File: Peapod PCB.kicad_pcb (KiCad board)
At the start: 2 copper layers, 70.9 x 26.9 mm, 20 parts, among them U1 ESP8266

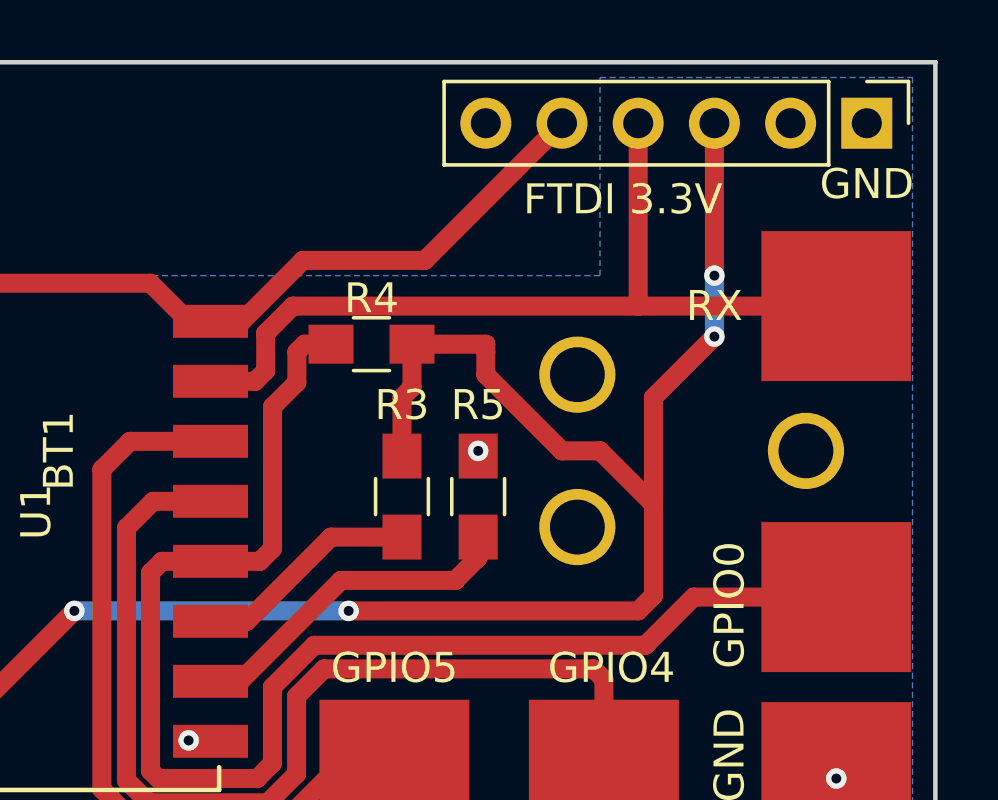
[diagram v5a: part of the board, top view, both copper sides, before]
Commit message: Moved Via
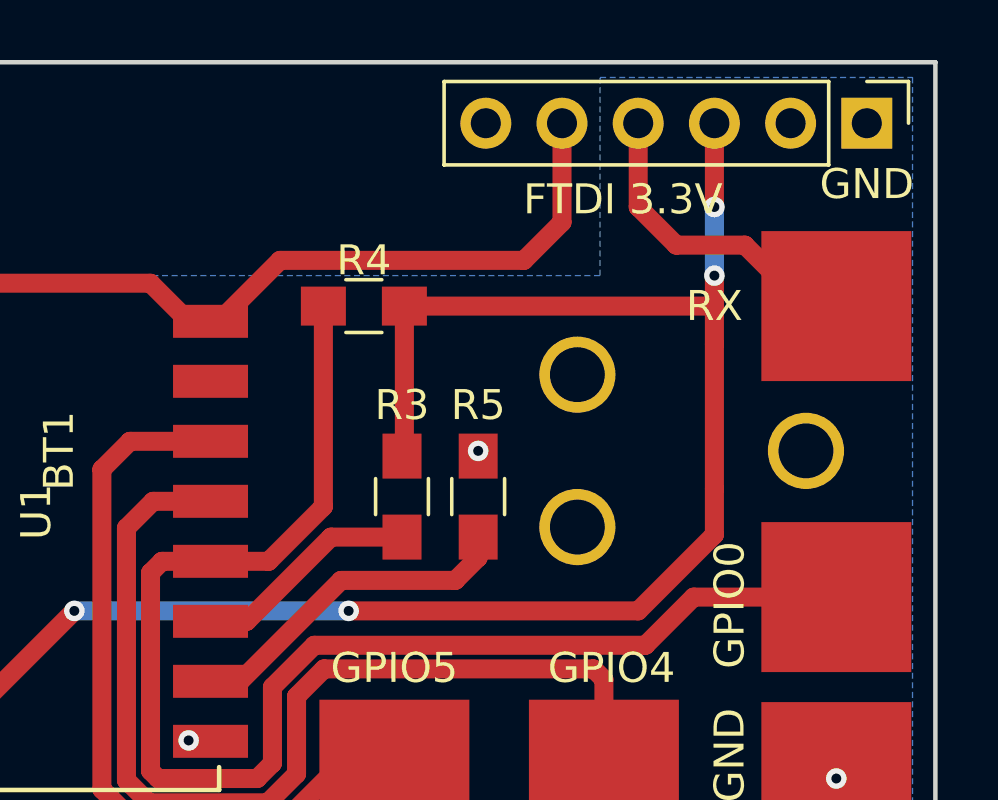
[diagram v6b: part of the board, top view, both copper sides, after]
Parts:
- moved R4 1.30 mm to (204.7, 34.5)
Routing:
- net Net-(J3-Pad4): track 30.7 -> 10.8 mm
- net Net-(J3-Pad5): track 41.9 -> 43.8 mm
- net +3V3: track 140.8 -> 141.7 mm
- net Net-(J7-Pad1): track 46.1 -> 46.9 mm
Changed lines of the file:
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@@
   (general
     (links 42)
-    (no_connects 0)
-    (area 150.970267 23.462266 225.457734 53.415001)
+    (no_connects 1)
+    (area 152.832999 26.340999 223.849001 53.415001)
     (thickness 1.6002)
     (drawings 9)
-    (tracks 157)
+    (tracks 147)
     (zones 0)
     (modules 20)
@@
   )
   (module Resistors_SMD:R_0805_HandSoldering (layer F.Cu)
-    (at 204.978 35.814)
+    (at 204.724 34.544)
     (descr "Resistor SMD 0805, hand soldering")
     (tags "resistor 0805")
@@
     (effects (font (size 6 7) (thickness 0.3)) (justify mirror))
   )
+  (segment (start 206.074 34.544) (end 216.408 34.544) (width 0.635) (layer F.Cu) (net 1) (status 400000))
+  (segment (start 216.408 34.544) (end 216.408 34.798) (width 0.635) (layer F.Cu) (net 1))
+  (segment (start 206.074 34.544) (end 206.074 39.464) (width 0.635) (layer F.Cu) (net 1) (status C00000))
+  (segment (start 206.074 39.464) (end 205.994 39.544) (width 0.635) (layer F.Cu) (net 1) (status C00000))
   (segment (start 184.912 49.052) (end 190.754 49.022) (width 0.635) (layer F.Cu) (net 1))
+  (segment (start 216.408 35.814) (end 216.408 34.798) (width 0.635) (layer F.Cu) (net 1))
+  (segment (start 216.408 40.64) (end 216.408 35.814) (width 0.635) (layer F.Cu) (net 1))
+  (segment (start 216.408 42.164) (end 216.408 40.64) (width 0.635) (layer F.Cu) (net 1))
+  (segment (start 213.868 44.704) (end 216.408 42.164) (width 0.635) (layer F.Cu) (net 1))
+  (segment (start 204.216 44.704) (end 213.868 44.704) (width 0.635) (layer F.Cu) (net 1))
+  (via (at 204.216 44.704) (size 0.6858) (drill 0.3302) (layers F.Cu B.Cu) (net 1))
+  (segment (start 195.072 44.704) (end 204.216 44.704) (width 0.635) (layer B.Cu) (net 1))
+  (via (at 195.072 44.704) (size 0.6858) (drill 0.3302) (layers F.Cu B.Cu) (net 1))
   (segment (start 190.754 49.022) (end 195.072 44.704) (width 0.635) (layer F.Cu) (net 1))
-  (via (at 195.072 44.704) (size 0.6858) (drill 0.3302) (layers F.Cu B.Cu) (net 1))
-  (segment (start 195.072 44.704) (end 204.216 44.704) (width 0.635) (layer B.Cu) (net 1))
-  (via (at 204.216 44.704) (size 0.6858) (drill 0.3302) (layers F.Cu B.Cu) (net 1))
-  (segment (start 204.216 44.704) (end 213.868 44.704) (width 0.635) (layer F.Cu) (net 1))
-  (segment (start 213.868 44.704) (end 214.376 44.196) (width 0.635) (layer F.Cu) (net 1))
-  (segment (start 214.376 44.196) (end 214.376 41.148) (width 0.635) (layer F.Cu) (net 1))
   (segment (start 163.96 41.91) (end 171.958 41.91) (width 0.635) (layer F.Cu) (net 1))
   (segment (start 174.816 39.052) (end 184.912 39.052) (width 0.635) (layer F.Cu) (net 1))
   (segment (start 171.958 41.91) (end 174.816 39.052) (width 0.635) (layer F.Cu) (net 1))
-  (segment (start 214.376 41.148) (end 214.376 37.592) (width 0.635) (layer F.Cu) (net 1))
-  (segment (start 214.376 37.592) (end 216.408 35.56) (width 0.635) (layer F.Cu) (net 1))
-  (via (at 216.408 35.56) (size 0.6858) (drill 0.3302) (layers F.Cu B.Cu) (net 1))
-  (segment (start 216.408 35.56) (end 216.408 33.528) (width 0.635) (layer B.Cu) (net 1))
+  (segment (start 216.408 34.798) (end 216.408 33.528) (width 0.635) (layer F.Cu) (net 1))
+  (segment (start 216.408 31.242) (end 216.408 28.448) (width 0.635) (layer F.Cu) (net 1) (status 800000))
+  (via (at 216.408 31.242) (size 0.6858) (drill 0.3302) (layers F.Cu B.Cu) (net 1))
+  (segment (start 216.408 33.528) (end 216.408 31.242) (width 0.635) (layer B.Cu) (net 1))
   (via (at 216.408 33.528) (size 0.6858) (drill 0.3302) (layers F.Cu B.Cu) (net 1))
-  (segment (start 216.408 33.528) (end 216.408 28.448) (width 0.635) (layer F.Cu) (net 1) (status 800000))
-  (segment (start 205.994 39.544) (end 205.994 37.592) (width 0.635) (layer F.Cu) (net 1))
-  (segment (start 206.328 37.258) (end 206.328 35.814) (width 0.635) (layer F.Cu) (net 1))
-  (segment (start 205.994 37.592) (end 206.328 37.258) (width 0.635) (layer F.Cu) (net 1))
-  (segment (start 208.788 35.814) (end 206.328 35.814) (width 0.635) (layer F.Cu) (net 1))
-  (segment (start 208.788 36.83) (end 208.788 36.068) (width 0.635) (layer F.Cu) (net 1))
-  (segment (start 211.328 39.37) (end 208.788 36.83) (width 0.635) (layer F.Cu) (net 1))
-  (segment (start 212.598 39.37) (end 211.328 39.37) (width 0.635) (layer F.Cu) (net 1))
-  (segment (start 214.376 41.148) (end 212.598 39.37) (width 0.635) (layer F.Cu) (net 1))
-  (segment (start 208.788 36.068) (end 208.788 35.814) (width 0.635) (layer F.Cu) (net 1))
   (segment (start 156.34 39.37) (end 156.34 39.748) (width 0.635) (layer F.Cu) (net 1))
   (segment (start 156.34 39.748) (end 155.194 40.894) (width 0.635) (layer F.Cu) (net 1))
@@
   (segment (start 179.578 35.052) (end 181.864 35.052) (width 0.635) (layer F.Cu) (net 7))
   (segment (start 181.864 35.052) (end 184.912 35.052) (width 0.635) (layer F.Cu) (net 7))
-  (segment (start 213.868 34.544) (end 202.356 34.544) (width 0.635) (layer F.Cu) (net 9))
-  (segment (start 201.098 37.052) (end 198.912 37.052) (width 0.635) (layer F.Cu) (net 9))
-  (segment (start 201.45 36.7) (end 201.098 37.052) (width 0.635) (layer F.Cu) (net 9))
-  (segment (start 201.45 35.45) (end 201.45 36.7) (width 0.635) (layer F.Cu) (net 9))
-  (segment (start 202.356 34.544) (end 201.45 35.45) (width 0.635) (layer F.Cu) (net 9))
-  (segment (start 213.868 34.544) (end 213.868 28.448) (width 0.635) (layer F.Cu) (net 9))
-  (segment (start 213.868 34.544) (end 220.472 34.544) (width 0.635) (layer F.Cu) (net 9))
-  (segment (start 220.472 34.544) (end 219.202 34.544) (width 0.635) (layer F.Cu) (net 9))
-  (segment (start 198.912 35.052) (end 200.66 35.052) (width 0.635) (layer F.Cu) (net 10))
-  (segment (start 200.66 35.052) (end 202.692 33.02) (width 0.635) (layer F.Cu) (net 10))
-  (segment (start 206.756 33.02) (end 211.328 28.448) (width 0.635) (layer F.Cu) (net 10))
-  (segment (start 202.692 33.02) (end 206.756 33.02) (width 0.635) (layer F.Cu) (net 10))
+  (segment (start 220.472 34.544) (end 219.456 34.544) (width 0.635) (layer F.Cu) (net 9) (status C00000))
+  (segment (start 219.456 34.544) (end 217.424 32.512) (width 0.635) (layer F.Cu) (net 9) (status 400000))
+  (segment (start 217.424 32.512) (end 215.138 32.512) (width 0.635) (layer F.Cu) (net 9))
+  (segment (start 215.138 32.512) (end 213.868 31.242) (width 0.635) (layer F.Cu) (net 9))
+  (segment (start 213.868 31.242) (end 213.868 28.448) (width 0.635) (layer F.Cu) (net 9) (status 800000))
+  (segment (start 198.912 35.052) (end 199.898 35.052) (width 0.635) (layer F.Cu) (net 10) (status C00000))
+  (segment (start 199.898 35.052) (end 201.93 33.02) (width 0.635) (layer F.Cu) (net 10) (status 400000))
+  (segment (start 211.328 31.75) (end 211.328 28.448) (width 0.635) (layer F.Cu) (net 10) (status 800000))
+  (segment (start 210.058 33.02) (end 211.328 31.75) (width 0.635) (layer F.Cu) (net 10))
+  (segment (start 201.93 33.02) (end 210.058 33.02) (width 0.635) (layer F.Cu) (net 10))
   (segment (start 174.498 29.464) (end 175.768 29.464) (width 0.635) (layer F.Cu) (net 10))
   (segment (start 175.768 29.464) (end 180.086 33.782) (width 0.635) (layer F.Cu) (net 10))
@@
   (segment (start 212.377402 46.637402) (end 203.396152 46.637402) (width 0.635) (layer F.Cu) (net 13))
   (segment (start 212.725 46.985) (end 212.377402 46.637402) (width 0.635) (layer F.Cu) (net 13))
-  (segment (start 203.628 35.814) (end 202.746 35.814) (width 0.635) (layer F.Cu) (net 14))
-  (segment (start 201.258 43.052) (end 198.912 43.052) (width 0.635) (layer F.Cu) (net 14))
-  (segment (start 201.68 42.63) (end 201.258 43.052) (width 0.635) (layer F.Cu) (net 14))
-  (segment (start 201.68 37.9) (end 201.68 42.63) (width 0.635) (layer F.Cu) (net 14))
-  (segment (start 202.49 37.09) (end 201.68 37.9) (width 0.635) (layer F.Cu) (net 14))
-  (segment (start 202.49 36.07) (end 202.49 37.09) (width 0.635) (layer F.Cu) (net 14))
-  (segment (start 202.746 35.814) (end 202.49 36.07) (width 0.635) (layer F.Cu) (net 14))
+  (segment (start 198.912 43.052) (end 201.55 43.052) (width 0.635) (layer F.Cu) (net 14) (status 400000))
+  (segment (start 203.374 41.228) (end 203.374 34.544) (width 0.635) (layer F.Cu) (net 14) (status 800000))
+  (segment (start 201.55 43.052) (end 203.374 41.228) (width 0.635) (layer F.Cu) (net 14))
   (segment (start 198.912 43.052) (end 197.994 43.052) (width 0.635) (layer F.Cu) (net 14))
   (segment (start 215.716 44.244) (end 220.472 44.244) (width 0.635) (layer F.Cu) (net 14) (status 20))

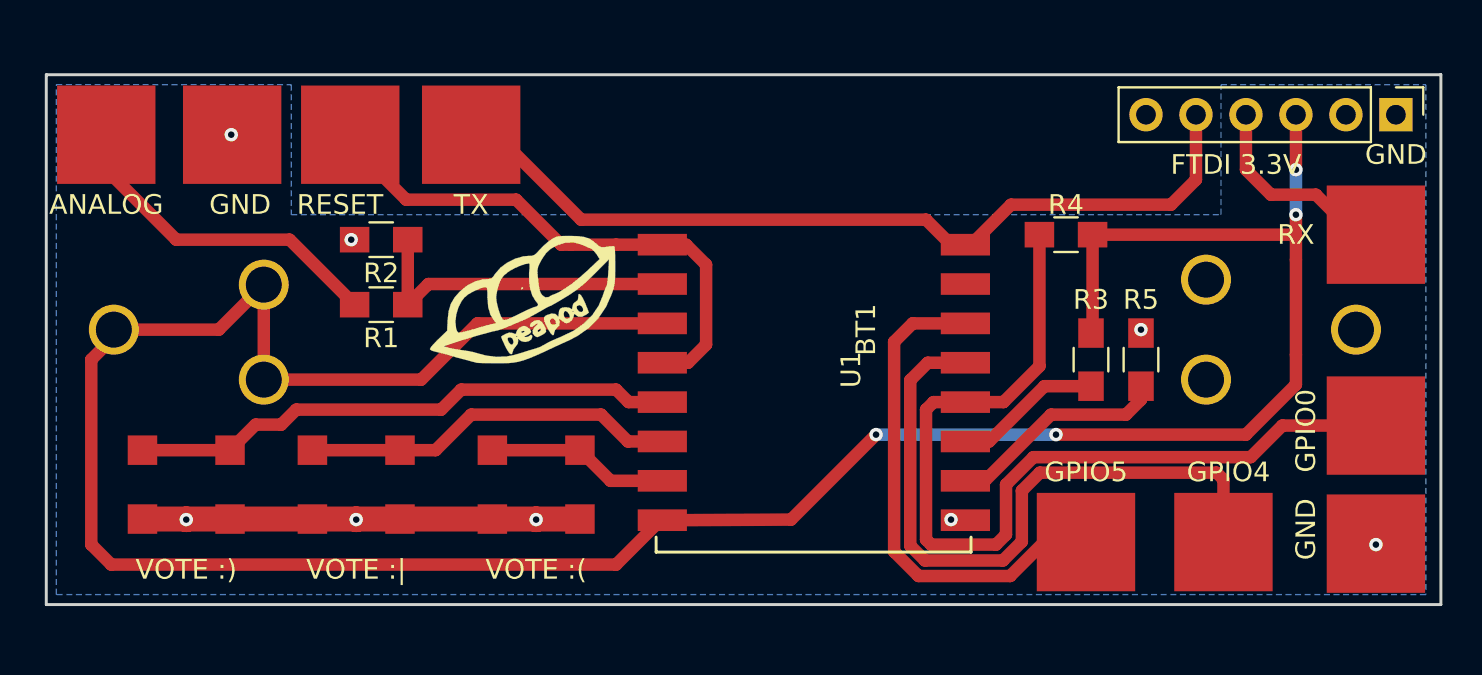
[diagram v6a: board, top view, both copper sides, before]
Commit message: Added gerbers and updated the silk screen
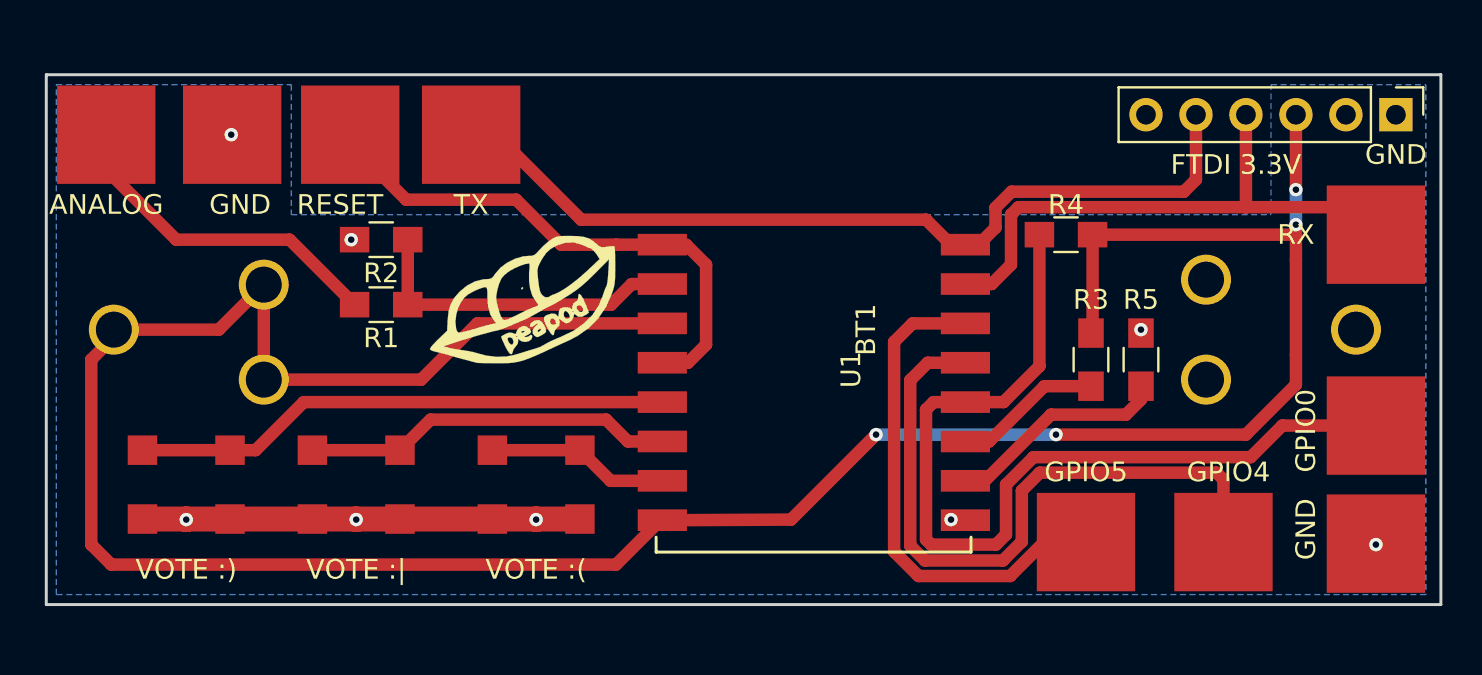
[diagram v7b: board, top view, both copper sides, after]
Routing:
- net Net-(J3-Pad4): track 10.8 -> 30.2 mm
- net Net-(J3-Pad5): track 43.8 -> 46.3 mm
- net Net-(BTN2-Pad2): track 28.7 -> 28.1 mm
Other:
- board text added: "2017"
- board text added: "FSOSS"
- board text removed: "FSOSS 2017"

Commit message: Updated Pads
Moved pads to the back layer
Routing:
- net Net-(J6-Pad1): track 33.8 -> 34.0 mm, vias 0 -> 1
- net Net-(J3-Pad5): vias 0 -> 1
- net Net-(J2-Pad1): vias 0 -> 1
- net Net-(J1-Pad1): vias 0 -> 1
- net Net-(J7-Pad1): vias 0 -> 1
- net Net-(J5-Pad1): vias 0 -> 1
- net Net-(J3-Pad4): vias 0 -> 1
- net GND: vias 8 -> 6
